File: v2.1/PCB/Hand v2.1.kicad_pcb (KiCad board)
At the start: 2 copper layers, 39 x 58 mm, 41 parts, among them J1 Conn_ARM_JTAG_SWD_10, M1 Index_Servo, M2 Middle_Servo, M3 Ring_Servo, M4 Pinky_Servo, M5 Thumb_Servo, SW1 Power_Switch, U1 STM32F303CCT7

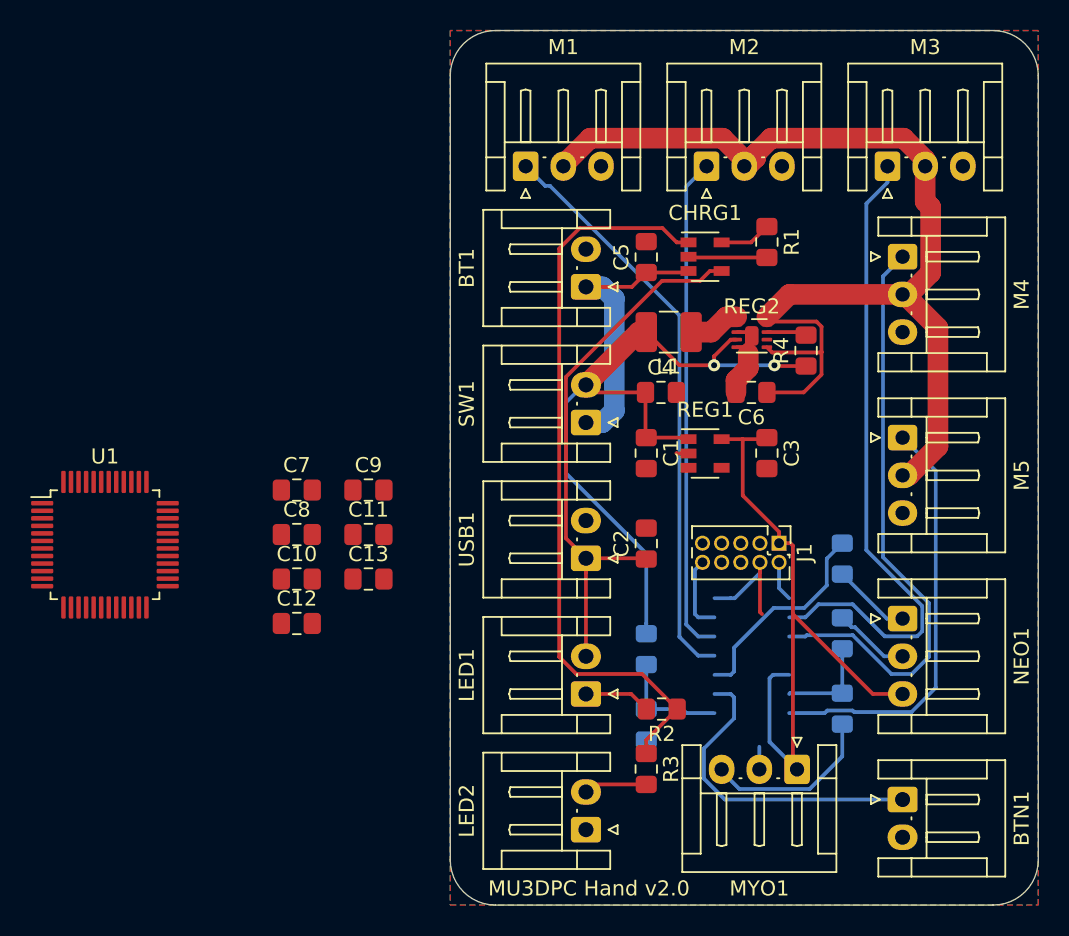
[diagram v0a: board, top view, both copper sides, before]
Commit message: finished adding STM32F303VCT6
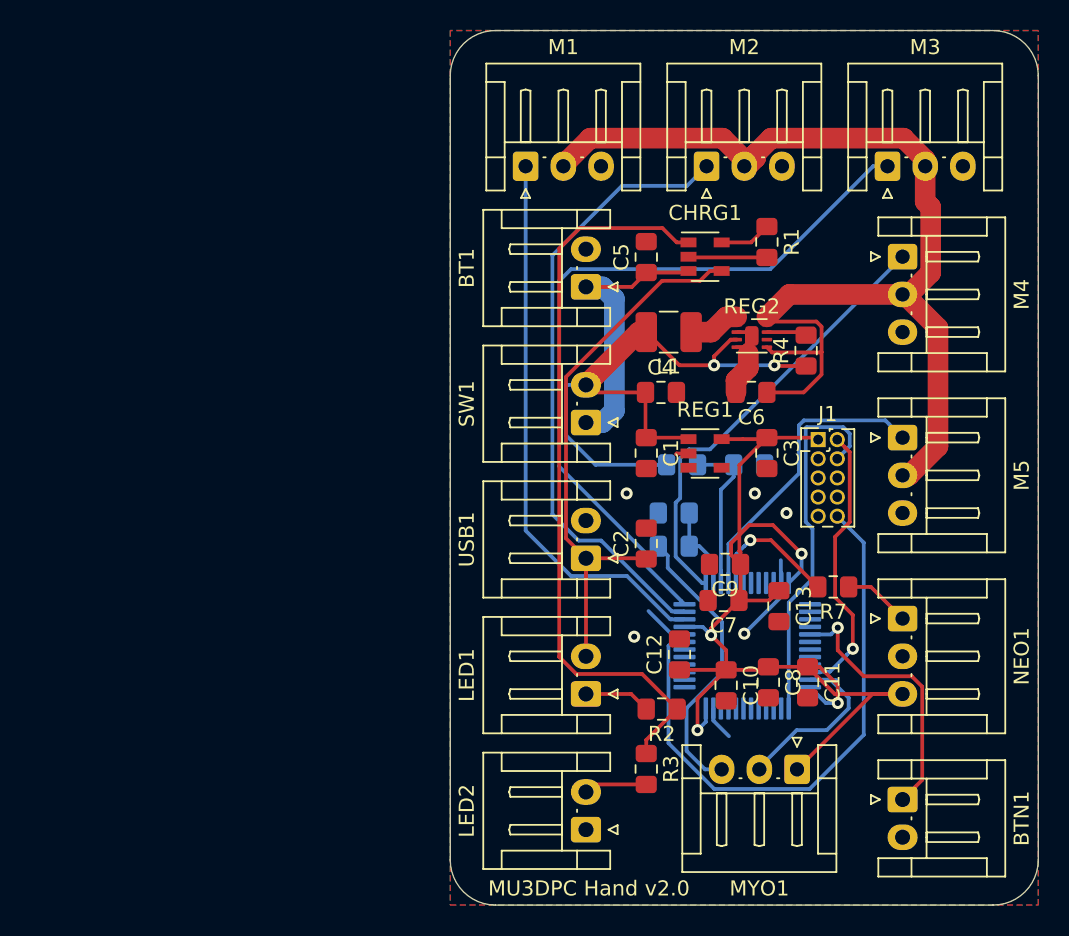
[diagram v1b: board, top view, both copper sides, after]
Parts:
- R7: moved to F.Cu
- U1: moved to B.Cu
- moved U1 43.1 mm to (132.7, 57.8)
- moved C8 32.8 mm to (134.1, 60.2), turned to 270 degrees
- moved C11 30.7 mm to (136.7, 60.2), turned to 270 degrees
- moved C10 29.3 mm to (131.3, 60.4), turned to 270 degrees
- moved C7 29.2 mm to (131.1, 54.8), turned to 180 degrees
- moved C13 27.3 mm to (134.8, 55.2), turned to 270 degrees
- moved C12 25.5 mm to (128.2, 58.4), turned to 90 degrees
- moved C9 24.2 mm to (131.2, 52.4), turned to 180 degrees
- moved R6 18.5 mm to (132.8, 45.8), turned to 0 degrees
- moved R8 15.5 mm to (127.8, 51.2), turned to 0 degrees
- moved R9 13.7 mm to (127.8, 49.0), turned to 180 degrees
- moved R5 12.5 mm to (128.4, 45.8), turned to 0 degrees
- moved J1 7.34 mm to (137.4, 44.1), turned to 0 degrees
- moved R7 1.97 mm to (138.4, 53.9), turned to 180 degrees
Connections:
- BTN1 pad 1: (no net) -> BTN
- M1 pad 1: (no net) -> INDEX
- M2 pad 1: (no net) -> MIDDLE
- M3 pad 1: (no net) -> RING
- M4 pad 1: (no net) -> PINKY
- M5 pad 1: (no net) -> THUMB
- R7 pad 2: (no net) -> NEO
- U1 pad 10: (no net) -> INDEX
- U1 pad 11: (no net) -> MIDDLE
- U1 pad 12: (no net) -> RING
- U1 pad 13: (no net) -> PINKY
- U1 pad 14: (no net) -> NORMMYOSIG
- U1 pad 15: (no net) -> NORMVBAT
- U1 pad 16: (no net) -> THUMB
- U1 pad 17: (no net) -> NEO
- U1 pad 29: (no net) -> BTN
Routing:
- net (no net): track 217.4 -> 0.00 mm
- net RING: track 0.00 -> 49.8 mm
- net MIDDLE: track 0.00 -> 41.3 mm
- net INDEX: track 0.00 -> 37.1 mm
- net Net-(J1-Pad10): track 5.03 -> 38.5 mm
- net +3V3: track 44.5 -> 75.8 mm, vias 0 -> 4
- net PINKY: track 0.00 -> 29.7 mm
- net THUMB: track 0.00 -> 19.9 mm
- net BTN: track 0.00 -> 18.1 mm, vias 0 -> 1
- net GND: track 12.8 -> 30.7 mm, vias 0 -> 5
- net Net-(J1-Pad4): track 7.90 -> 24.6 mm
- net Net-(J1-Pad2): track 2.66 -> 18.6 mm, vias 0 -> 1
- net NEO: track 0.00 -> 8.99 mm, vias 0 -> 1
- net MYOSIG: track 11.6 -> 19.1 mm
- net +BATT: track 49.4 -> 42.2 mm
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
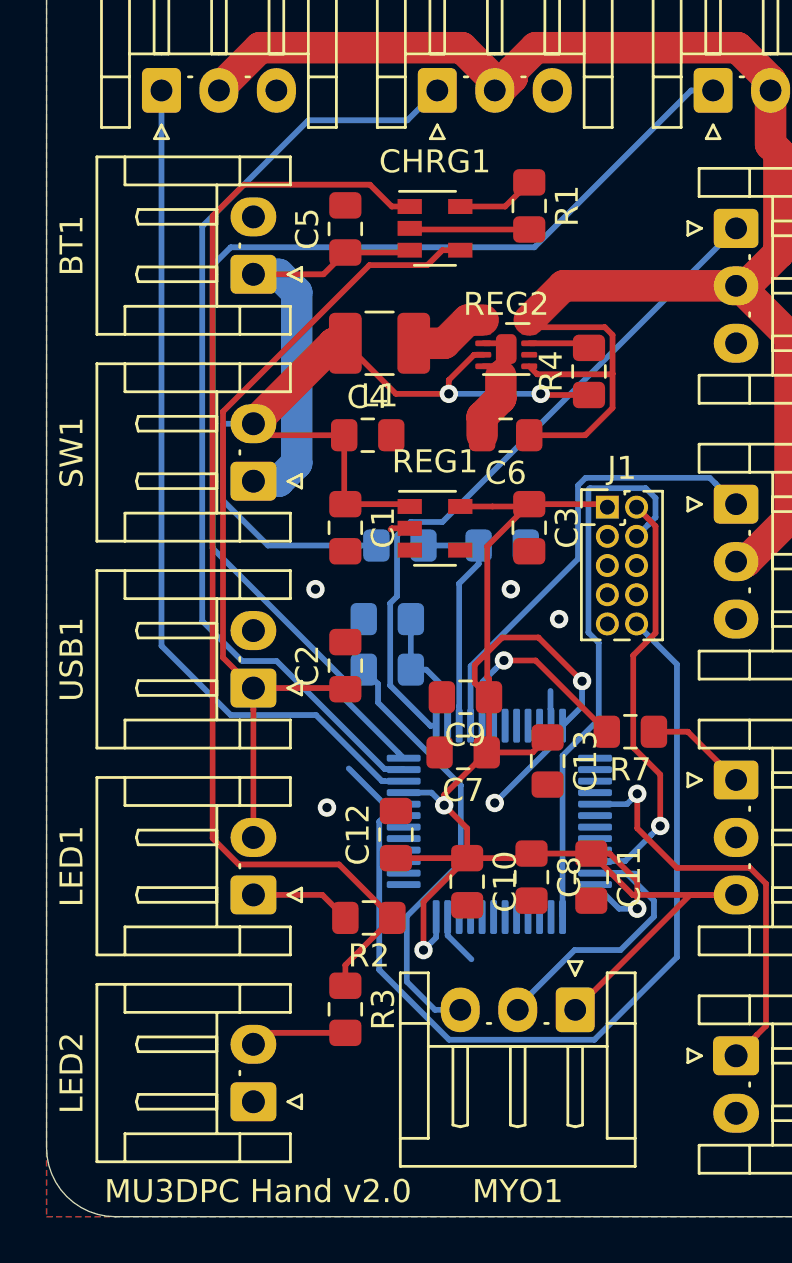
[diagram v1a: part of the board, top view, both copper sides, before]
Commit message: cleaned up silkscreen and updated version on silkscreen
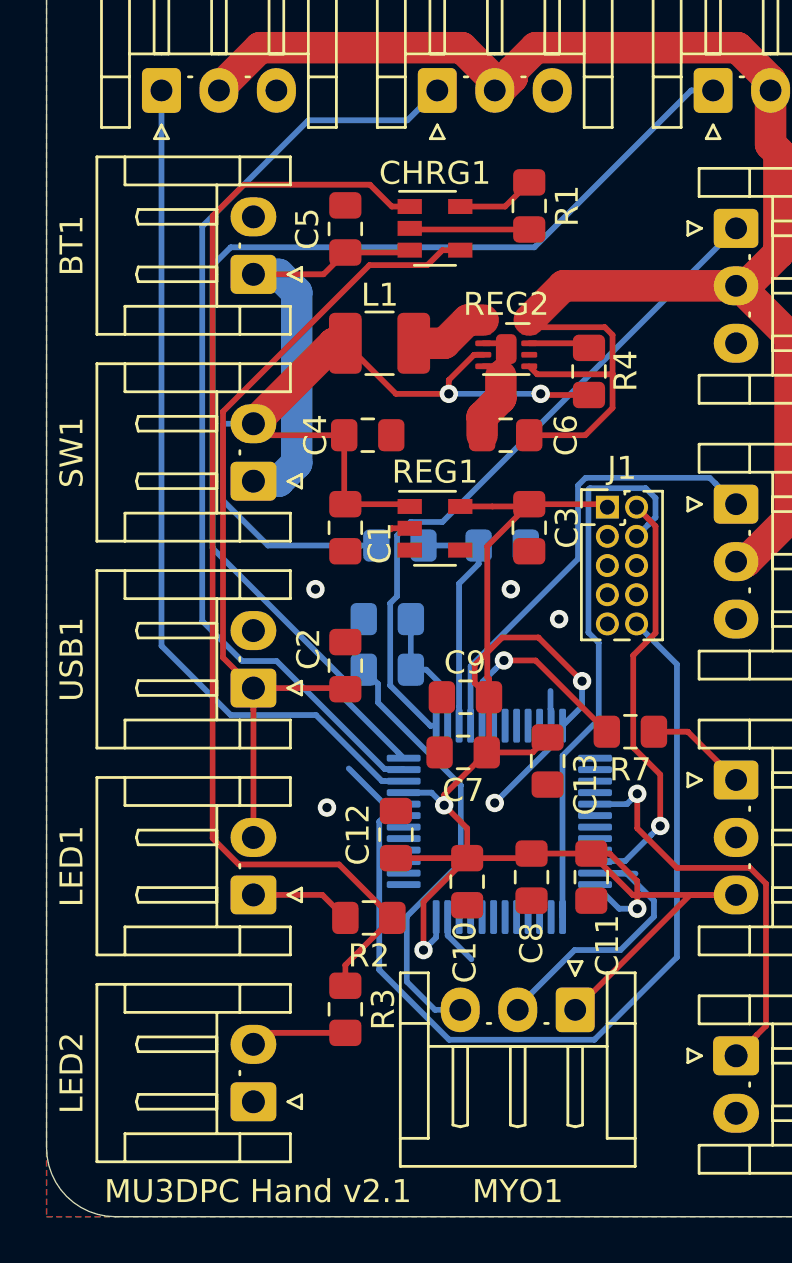
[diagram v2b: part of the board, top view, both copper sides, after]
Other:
- board text added: "MU3DPC Hand v2.1"
- board text removed: "MU3DPC Hand v2.0"
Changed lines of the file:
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@@
     (tags "capacitor handsolder")
     (attr smd)
-    (fp_text reference C1 (at 0 -1.65 90) (layer F.SilkS)
+    (fp_text reference C1 (at 0.675 -1.5 90) (layer F.SilkS)
       (effects (font (size 1 1) (thickness 0.15)))
     )
@@
     (tags "capacitor handsolder")
     (attr smd)
-    (fp_text reference C2 (at 0 -1.65 90) (layer F.SilkS)
+    (fp_text reference C2 (at 0.725 -1.6 90) (layer F.SilkS)
       (effects (font (size 1 1) (thickness 0.15)))
     )
@@
     (tags "capacitor handsolder")
     (attr smd)
-    (fp_text reference C4 (at 0 -1.65) (layer F.SilkS)
+    (fp_text reference C4 (at -2.275 0 90) (layer F.SilkS)
       (effects (font (size 1 1) (thickness 0.15)))
     )
@@
     (tags "capacitor handsolder")
     (attr smd)
-    (fp_text reference C6 (at 0 -1.65) (layer F.SilkS)
+    (fp_text reference C6 (at -2.625 0 90) (layer F.SilkS)
       (effects (font (size 1 1) (thickness 0.15)))
     )
@@
     (tags SOT-23-5)
     (attr smd)
-    (fp_text reference CHRG1 (at 0 -2.9) (layer F.SilkS)
+    (fp_text reference CHRG1 (at 0 -2.4) (layer F.SilkS)
       (effects (font (size 1 1) (thickness 0.15)))
     )
@@
     (tags "inductor handsolder")
     (attr smd)
-    (fp_text reference L1 (at 0 -2.28) (layer F.SilkS)
+    (fp_text reference L1 (at -0.0125 2.1) (layer F.SilkS)
       (effects (font (size 1 1) (thickness 0.15)))
     )
@@
     (tags "resistor handsolder")
     (attr smd)
-    (fp_text reference R4 (at 0 -1.65 90) (layer F.SilkS)
+    (fp_text reference R4 (at 0.025 1.6 90) (layer F.SilkS)
       (effects (font (size 1 1) (thickness 0.15)))
     )
@@
     (tags "resistor handsolder")
     (attr smd)
-    (fp_text reference R5 (at 0 1.65 180) (layer B.SilkS)
+    (fp_text reference R5 (at 0.025 -1.4 180) (layer B.SilkS)
       (effects (font (size 1 1) (thickness 0.15)) (justify mirror))
     )
@@
     (tags "resistor handsolder")
     (attr smd)
-    (fp_text reference R9 (at 0 1.65 180) (layer B.SilkS)
+    (fp_text reference R9 (at 2.425 0.1 270) (layer B.SilkS)
       (effects (font (size 1 1) (thickness 0.15)) (justify mirror))
     )
@@
     (tags SOT-23-5)
     (attr smd)
-    (fp_text reference REG1 (at 0 -2.9) (layer F.SilkS)
+    (fp_text reference REG1 (at 0 -2.45) (layer F.SilkS)
       (effects (font (size 1 1) (thickness 0.15)))
     )
@@
     (tags "capacitor handsolder")
     (attr smd)
-    (fp_text reference C8 (at 0 -1.65 270) (layer F.SilkS)
+    (fp_text reference C8 (at 2.875 0 270) (layer F.SilkS)
       (effects (font (size 1 1) (thickness 0.15)))
     )
@@
     (tags "capacitor handsolder")
     (attr smd)
-    (fp_text reference C9 (at 0 -1.65 180) (layer F.SilkS)
+    (fp_text reference C9 (at 0.025 1.5 180) (layer F.SilkS)
       (effects (font (size 1 1) (thickness 0.15)))
     )
@@
     (tags "capacitor handsolder")
     (attr smd)
-    (fp_text reference C10 (at 0 -1.65 90) (layer F.SilkS)
+    (fp_text reference C10 (at 3.075 0.1 90) (layer F.SilkS)
       (effects (font (size 1 1) (thickness 0.15)))
     )
@@
     (tags "capacitor handsolder")
     (attr smd)
-    (fp_text reference C11 (at 0 -1.65 270) (layer F.SilkS)
+    (fp_text reference C11 (at 2.975 -0.7 270) (layer F.SilkS)
       (effects (font (size 1 1) (thickness 0.15)))
     )
@@
     (tags "capacitor handsolder")
     (attr smd)
-    (fp_text reference C13 (at 0 -1.65 270) (layer F.SilkS)
+    (fp_text reference C13 (at 1.025 -1.65 270) (layer F.SilkS)
       (effects (font (size 1 1) (thickness 0.15)))
     )
@@
     )
   )
-  (gr_text "MU3DPC Hand v2.0" (at 122.2 73.9) (layer F.SilkS)
+  (gr_text "MU3DPC Hand v2.1" (at 122.2 73.9) (layer F.SilkS)
     (effects (font (size 1 1) (thickness 0.15)))
   )
@@
   (segment (start 134.95 54.55) (end 132.5 57) (width 0.25) (layer B.Cu) (net 1))
   (segment (start 134.95 53.6375) (end 134.95 54.55) (width 0.25) (layer B.Cu) (net 1))
-  (via (at 138.7 56.6) (size 0.8) (drill 0.4) (layers F.Cu B.Cu) (net 21))
-  (via (at 129.4 63.4) (size 0.8) (drill 0.4) (layers F.Cu B.Cu) (net 5))
-  (via (at 130.3 57.1) (size 0.8) (drill 0.4) (layers F.Cu B.Cu) (net 5))
-  (via (at 138.7 61.6) (size 0.8) (drill 0.4) (layers F.Cu B.Cu) (net 5))
-  (via (at 136.3 51.7) (size 0.8) (drill 0.4) (layers F.Cu B.Cu) (net 5))
-  (via (at 139.7 58) (size 0.8) (drill 0.4) (layers F.Cu B.Cu) (net 10))
-  (via (at 132.9 50.8) (size 0.8) (drill 0.4) (layers F.Cu B.Cu) (net 27))
   (segment (start 125.05 34) (end 126 33.05) (width 0.25) (layer F.Cu) (net 2))
   (segment (start 122 34) (end 125.05 34) (width 0.25) (layer F.Cu) (net 2))
@@
   (segment (start 122 52.95) (end 122 58.5) (width 0.25) (layer F.Cu) (net 4))
   (segment (start 122 52) (end 122 52.95) (width 0.25) (layer F.Cu) (net 4))
+  (via (at 129.4 63.4) (size 0.8) (drill 0.4) (layers F.Cu B.Cu) (net 5))
+  (via (at 130.3 57.1) (size 0.8) (drill 0.4) (layers F.Cu B.Cu) (net 5))
+  (via (at 138.7 61.6) (size 0.8) (drill 0.4) (layers F.Cu B.Cu) (net 5))
+  (via (at 136.3 51.7) (size 0.8) (drill 0.4) (layers F.Cu B.Cu) (net 5))
   (segment (start 133.9 44.1) (end 134 44) (width 0.25) (layer F.Cu) (net 5))
   (segment (start 131 44.1) (end 132.4 44.1) (width 0.25) (layer F.Cu) (net 5))
@@
   (segment (start 125.72501 59.67501) (end 121.363295 59.67501) (width 0.25) (layer F.Cu) (net 9))
   (segment (start 128.05 62) (end 125.72501 59.67501) (width 0.25) (layer F.Cu) (net 9))
+  (via (at 139.7 58) (size 0.8) (drill 0.4) (layers F.Cu B.Cu) (net 10))
   (segment (start 139.300001 58.399999) (end 139.7 58) (width 0.25) (layer B.Cu) (net 10))
   (segment (start 138.17499 59.52501) (end 139.300001 58.399999) (width 0.25) (layer B.Cu) (net 10))
@@
   (segment (start 140.9 53.9) (end 143 56) (width 0.25) (layer F.Cu) (net 20))
   (segment (start 139.425 53.9) (end 140.9 53.9) (width 0.25) (layer F.Cu) (net 20))
+  (via (at 138.7 56.6) (size 0.8) (drill 0.4) (layers F.Cu B.Cu) (net 21))
   (segment (start 138.25 57.05) (end 138.7 56.6) (width 0.25) (layer B.Cu) (net 21))
   (segment (start 136.8625 57.05) (end 138.25 57.05) (width 0.25) (layer B.Cu) (net 21))
@@
   (segment (start 131.45 51.05) (end 136.124989 46.375011) (width 0.25) (layer B.Cu) (net 26))
   (segment (start 131.45 53.6375) (end 131.45 51.05) (width 0.25) (layer B.Cu) (net 26))
+  (via (at 132.9 50.8) (size 0.8) (drill 0.4) (layers F.Cu B.Cu) (net 27))
   (segment (start 132.500001 51.199999) (end 132.9 50.8) (width 0.25) (layer B.Cu) (net 27))
   (segment (start 131.97499 51.72501) (end 132.500001 51.199999) (width 0.25) (layer B.Cu) (net 27))

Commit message: connected unused IO pins on MCU to ground
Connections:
- U1 pad 18: (no net) -> GND
- U1 pad 19: (no net) -> GND
- U1 pad 2: (no net) -> GND
- U1 pad 20: (no net) -> GND
- U1 pad 21: (no net) -> GND
- U1 pad 22: (no net) -> GND
- U1 pad 25: (no net) -> GND
- U1 pad 26: (no net) -> GND
- U1 pad 27: (no net) -> GND
- U1 pad 28: (no net) -> GND
- U1 pad 3: (no net) -> GND
- U1 pad 30: (no net) -> GND
- U1 pad 31: (no net) -> GND
- U1 pad 32: (no net) -> GND
- U1 pad 33: (no net) -> GND
- U1 pad 38: (no net) -> GND
- U1 pad 39: (no net) -> GND
- U1 pad 4: (no net) -> GND
- U1 pad 40: (no net) -> GND
- U1 pad 41: (no net) -> GND
- U1 pad 42: (no net) -> GND
- U1 pad 43: (no net) -> GND
- U1 pad 44: (no net) -> GND
- U1 pad 45: (no net) -> GND
- U1 pad 46: (no net) -> GND
- U1 pad 5: (no net) -> GND
- U1 pad 6: (no net) -> GND
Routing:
- net GND: track 30.7 -> 63.0 mm, vias 5 -> 6
